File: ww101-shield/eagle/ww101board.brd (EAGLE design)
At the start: 64.5 x 73.1 mm, 62 parts

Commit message: before library update
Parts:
- added C15, C16, C17: 0.1uF, PatternAgents-ProtoPads:0603-CAP
- added R25: 0R, PatternAgents-ProtoPads:0603-RES
- moved C3 0.71 mm to (13.5, 17.8)
- moved C4 0.56 mm to (14.9, 17.8)
- moved R22 0.43 mm to (30.0, 11.7)
- moved C7 0.41 mm to (16.3, 17.8)
- moved C8 0.25 mm to (17.7, 17.8)
- moved C6 0.23 mm to (23.9, 1.52)
- moved C13 0.20 mm to (19.2, 1.78)
- moved C12 0.20 mm to (21.9, 17.8)
- moved C9 0.10 mm to (19.1, 17.8)
- moved C5 0.08 mm to (22.5, 1.52)
- moved D1 0.07 mm to (20.8, 3.10)
- moved C14 0.05 mm to (20.5, 17.8)
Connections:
- removed net VPWR: C1.2, C2.2, C3.2, C4.2, C5.1, C6.1, C8.2, C9.2, CLED0.A, CLED1.A, CLED2.A, CLED3.A, D1.ANNODE, JMP1.2, JP1.5, JPWR.2, LED1.A, LED2.A, PROX.A, R10.1, R18.2, R19.2, R2.3, R20.2, R21.2, R22.1, R30.1, R31.3, R9.1, U$7.19, U$7.43, U$7.47, U$7.8
- new net CAP-PSOC: R25.2, U$7.15
- new net VCC: C1.2, C15.1, C17.1, C2.2, C3.2, C4.2, C5.1, C6.1, C8.2, C9.2, CLED0.A, CLED1.A, CLED2.A, CLED3.A, D1.ANNODE, JMP1.2, JP1.5, JPWR.2, LED1.A, LED2.A, PROX.A, R10.1, R18.2, R19.2, R2.3, R20.2, R21.2, R22.1, R30.1, R31.3, R9.1, U$7.19, U$7.43, U$7.47, U$7.8
- net CAP-PROX: now also R25.1; no longer U$7.15
- net GND: now also C16.2, C17.2
- net POT: now also C16.1
- net XRES: now also C15.2
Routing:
- net VCC: track 0.00 -> 215.6 mm, vias 0 -> 2
- net VPWR: track 213.5 -> 0.00 mm, vias 2 -> 0
- net CAP-PROX: track 278.4 -> 268.3 mm
- net CAP-PSOC: track 0.00 -> 8.86 mm
- net POT: track 135.0 -> 138.5 mm
- net VDAC: track 105.2 -> 108.0 mm
- net XRES: track 74.5 -> 76.6 mm
- net GND: track 81.6 -> 81.1 mm, vias 94 -> 100

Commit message: the saturday night checkin of all of the V2.1 changes
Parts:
- removed JMP1: 0, PatternAgents-ProtoPads:JMP-3-NO-PTH-2.54
- removed JP1: 0, SparkFun-Connectors:1X05_LOCK
- removed JPWR: 0, PatternAgents-ProtoPads:JMP-3-NO-0603
- removed U$2: U8G-096-OLED, IOTExpert:096-SSD1306
- added J5: (no value), ww101board:JMP-3-NO-PTH-2.54
- added J6: U8G-096-OLED, ww101board:096-SSD1306
- added J7: 0, ww101board:1X05_LOCK
- added R32: (no value), ww101board:JMP-3-NO
- B0, B1, B2, B3: device PatternAgents-TouchWidgets:BUTTON_PASSIVE_10MM -> ww101board:BUTTON_PASSIVE_10MM
- C1, C10, C11, C12, C13, C14, C15, C16, C17, C2, C3, C4, C5, C6, C7, C8, C9: device PatternAgents-ProtoPads:0603-CAP -> ww101board:0603-CAP
- CLED0, CLED1, CLED2, CLED3, LED1, LED2, PROX: device adafruit:CHIP-LED0603 -> ww101board:CHIP-LED0603
- D1: device IOTExpert:ALS -> ww101board:ALS
- HUMIDITY: device IOTExpert:HUMIDITY -> ww101board:HUMIDITY
- MB1, MB2: device IOTExpert:SWITCH -> ww101board:SWITCH
- R1, R10, R12, R13, R14, R15, R16, R17, R18, R19, R20, R21, R22, R23, R24, R25, R3, R4, R5, R6, R7, R8, R9: device PatternAgents-ProtoPads:0603-RES -> ww101board:0603-RES
- R11: device varistor:R-5 -> ww101board:R-5
- R2: device pot:3386P -> ww101board:3386P
- R30: device PatternAgents-ProtoPads:JMP-3-1_2 -> ww101board:JMP-3-1_2
- R31: device PatternAgents-ProtoPads:JMP-3-2_3 -> ww101board:JMP-3-2_3
- U$1: device SparkFun-Boards:UNO_R3_SHIELD_NOLABELS -> ww101board:UNO_R3_SHIELD_NOLABELS
- U$7: device PatternAgents-Cypress:TQFP-7X7-48 -> ww101board:TQFP-7X7-48
- moved R18 0.13 mm to (14.8, 39.4)
- moved C5 0.08 mm to (22.5, 1.45)
- moved C6 0.08 mm to (23.9, 1.45)
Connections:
- net GND: now also J7.4; no longer JP1.4
- net MB1: now also J7.1; no longer JP1.1
- net MB2: now also J7.2; no longer JP1.2
- net N$14: now also J6.VDD; no longer U$2.VDD
- net N$17: now also J6.GND; no longer U$2.GND
- net SCL: now also J6.SCL; no longer U$2.SCL
- net SDA: now also J6.SDA; no longer U$2.SDA
- net V33: now also J5.3, R32.1; no longer JMP1.3, JPWR.3
- net V50: now also J5.1, R32.3; no longer JMP1.1, JPWR.1
- net VCC: now also J5.2, J7.5, R32.2; no longer JMP1.2, JP1.5, JPWR.2
- net XRES: now also J7.3; no longer JP1.3
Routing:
- net GND: track 81.1 -> 78.2 mm
- net V33: track 20.2 -> 18.4 mm
- net VCC: track 215.6 -> 217.1 mm
- net THERM-REF-HIGH: track 26.0 -> 27.2 mm
- added copper zone on layer 1, net V33
- added copper zone on layer 1, net V50
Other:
- board size 64.5 x 73.1 mm -> 64.8 x 73.3 mm
- board text added: "J1"
- board text added: "J2"
- board text added: "J3"
- board text added: "J4"
- board text added: "J6"
- board text added: "PSoC AFE Shield V2.1"
- board text removed: "PSoC AFE Shield V2.0"

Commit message: a bunch of minor tweaks
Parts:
- C17: value 0.1uF -> 10uF
- renumbered U$7 to U7
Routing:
- net V33: track 18.4 -> 22.3 mm
- net V50: track 20.7 -> 22.5 mm

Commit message: a bunch of updates
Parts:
- removed U$3: (no value), IOTExpert:CYPRESSLOGO
- added U$7: CYLOGO-SILK, ww101board:CYLOGO-SILK
- R18, R19, R20, R21: value 4.7K -> DNP
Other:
- board size 64.8 x 73.3 mm -> 65.8 x 74.3 mm
- board text added: "600-60500-01 REV2.1"
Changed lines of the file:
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@@
 <layer number="17" name="Pads" color="2" fill="1" visible="yes" active="yes"/>
 <layer number="18" name="Vias" color="2" fill="1" visible="yes" active="yes"/>
-<layer number="19" name="Unrouted" color="6" fill="1" visible="yes" active="yes"/>
-<layer number="20" name="Dimension" color="15" fill="1" visible="yes" active="yes"/>
+<layer number="19" name="Unrouted" color="6" fill="1" visible="no" active="yes"/>
+<layer number="20" name="Dimension" color="15" fill="1" visible="no" active="yes"/>
 <layer number="21" name="tPlace" color="7" fill="1" visible="yes" active="yes"/>
 <layer number="22" name="bPlace" color="7" fill="1" visible="yes" active="yes"/>
@@
 <board>
 <plain>
-<wire x1="-5.7404" y1="-9.1694" x2="59.055" y2="-9.1694" width="0" layer="20"/>
-<wire x1="59.055" y1="-9.1694" x2="59.055" y2="64.135" width="0" layer="20"/>
-<wire x1="59.055" y1="64.135" x2="-5.7404" y2="64.135" width="0" layer="20"/>
-<wire x1="-5.7404" y1="64.135" x2="-5.7404" y2="-9.1694" width="0" layer="20"/>
+<wire x1="-6.2484" y1="-9.6774" x2="59.563" y2="-9.6774" width="0" layer="20"/>
+<wire x1="59.563" y1="-9.6774" x2="59.563" y2="64.643" width="0" layer="20"/>
+<wire x1="59.563" y1="64.643" x2="-6.2484" y2="64.643" width="0" layer="20"/>
+<wire x1="-6.2484" y1="64.643" x2="-6.2484" y2="-9.6774" width="0" layer="20"/>
 <text x="36.164521875" y="24.462740625" size="1.016" layer="25" font="vector" ratio="15" rot="R90">V33</text>
 <text x="55.095140625" y="27.040840625" size="1.016" layer="25" font="vector" ratio="15" rot="R180">V33</text>
@@
 <wire x1="20.7797375" y1="-1.33858125" x2="20.99818125" y2="-1.33858125" width="0.1524" layer="21"/>
 <wire x1="20.99818125" y1="-1.33858125" x2="21.638259375" y2="-1.978659375" width="0.1524" layer="21"/>
+<text x="17.266921875" y="-7.929884375" size="1.27" layer="26" ratio="10" rot="MR0">600-60500-01 REV2.1</text>
 </plain>
 <attributes>
@@
 <attribute name="VALUE" x="21.5138" y="16.2306" size="0.6096" layer="27" font="vector" ratio="15" rot="R90" align="top-left"/>
 </element>
-<element name="R18" library="ww101board" package="0603-RES" value="4.7K" x="14.7574" y="39.4208" smashed="yes">
+<element name="R18" library="ww101board" package="0603-RES" value="DNP" x="14.7574" y="39.4208" smashed="yes">
 <attribute name="NAME" x="16.494759375" y="40.8914625" size="0.8128" layer="25" font="vector" ratio="15" rot="R270"/>
 <attribute name="VALUE" x="13.2334" y="37.7698" size="0.6096" layer="27" font="vector" ratio="15"/>
 </element>
-<element name="R19" library="ww101board" package="0603-RES" value="4.7K" x="14.732" y="35.6362" locked="yes" smashed="yes" rot="MR180">
+<element name="R19" library="ww101board" package="0603-RES" value="DNP" x="14.732" y="35.6362" locked="yes" smashed="yes" rot="MR180">
 <attribute name="NAME" x="10.7188" y="35.8902" size="0.8128" layer="26" font="vector" ratio="15" rot="MR180"/>
 <attribute name="VALUE" x="13.208" y="37.2872" size="0.6096" layer="28" font="vector" ratio="15" rot="MR180"/>
 </element>
-<element name="R20" library="ww101board" package="0603-RES" value="4.7K" x="14.7574" y="38.0238" locked="yes" smashed="yes">
+<element name="R20" library="ww101board" package="0603-RES" value="DNP" x="14.7574" y="38.0238" locked="yes" smashed="yes">
 <attribute name="NAME" x="17.205959375" y="35.829240625" size="0.8128" layer="25" font="vector" ratio="15" rot="R90"/>
 <attribute name="VALUE" x="13.2334" y="36.3728" size="0.6096" layer="27" font="vector" ratio="15"/>
 </element>
-<element name="R21" library="ww101board" package="0603-RES" value="4.7K" x="14.732" y="36.8554" locked="yes" smashed="yes" rot="MR180">
+<element name="R21" library="ww101board" package="0603-RES" value="DNP" x="14.732" y="36.8554" locked="yes" smashed="yes" rot="MR180">
 <attribute name="NAME" x="10.6426" y="37.1856" size="0.8128" layer="26" font="vector" ratio="15" rot="MR180"/>
 <attribute name="VALUE" x="13.208" y="38.5064" size="0.6096" layer="28" font="vector" ratio="15" rot="MR180"/>
 </element>
 <element name="U$1" library="ww101board" package="UNO_R3_SHIELD_NOLABELS" value="ARDUINO_R3_SHIELDNOLABELS" x="-0.03" y="0.01" locked="yes"/>
-<element name="U$3" library="IOTExpert" package="CYPRESSLOGO" value="" x="52.0573" y="7.2009" rot="R90"/>
 <element name="R22" library="ww101board" package="0603-RES" value="10K" x="29.96691875" y="11.69161875" smashed="yes" rot="R180">
 <attribute name="NAME" x="31.1023" y="13.243559375" size="0.8128" layer="25" font="vector" ratio="15" rot="R180"/>
@@
 <attribute name="VALUE" x="37.337996875" y="28.26511875" size="0.6096" layer="27" font="vector" ratio="15" rot="R90"/>
 </element>
+<element name="U$7" library="ww101board" package="CYLOGO-SILK" value="CYLOGO-SILK" x="58.399678125" y="-8.453115625" rot="R90"/>
 </elements>
 <signals>

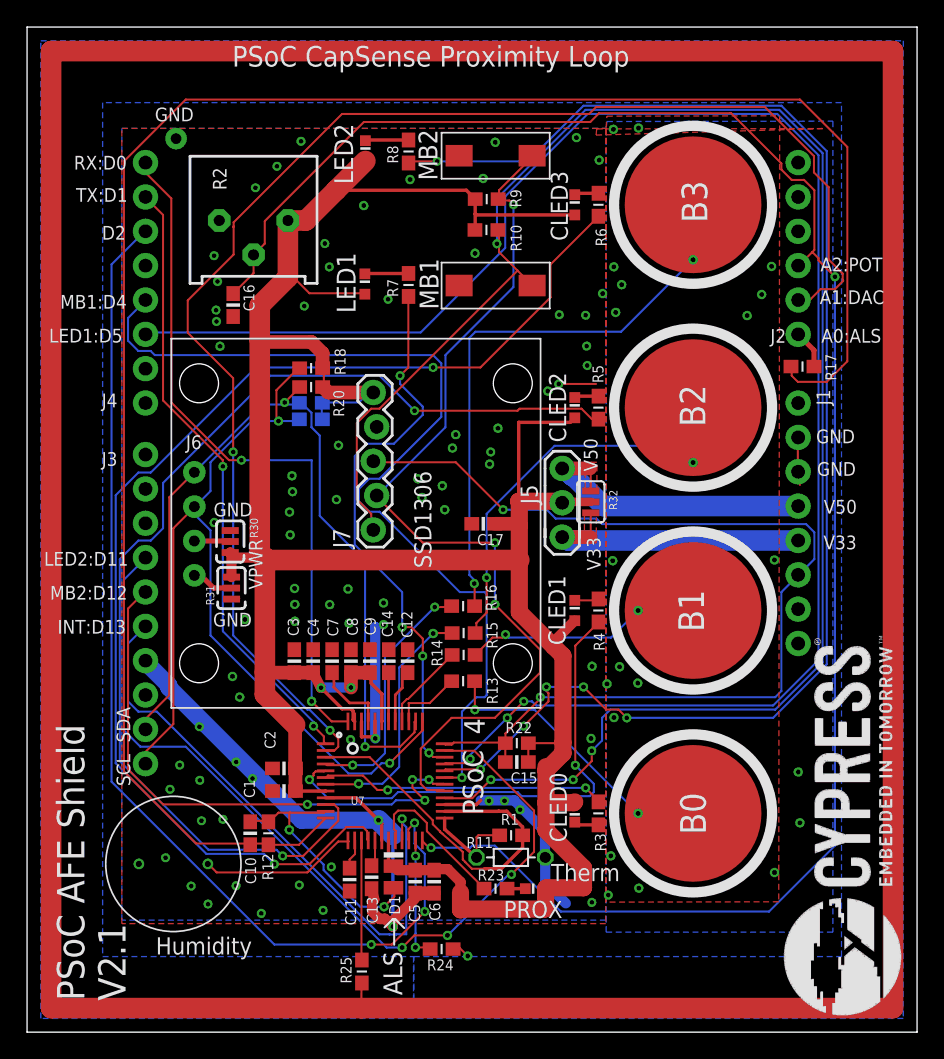
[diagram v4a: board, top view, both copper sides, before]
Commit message: updates to 2.1 board based on GJL inputs
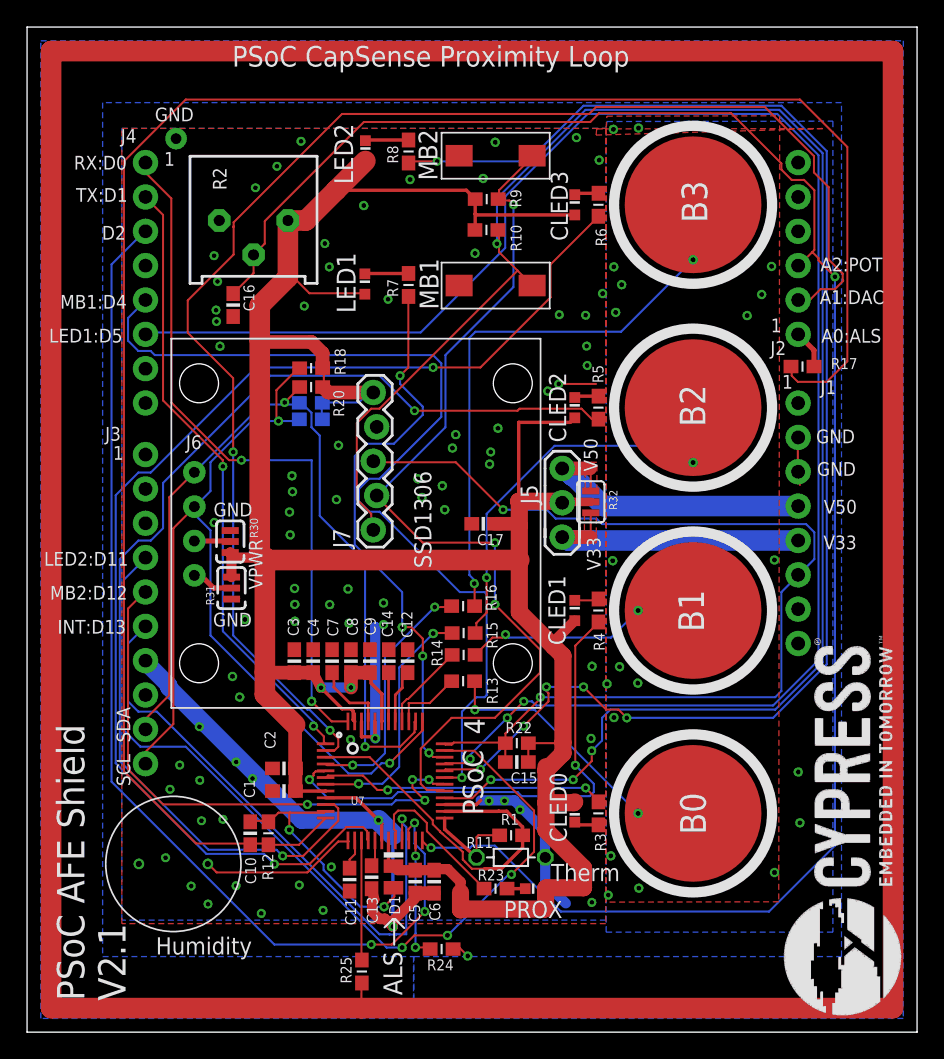
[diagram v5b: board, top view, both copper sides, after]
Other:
- board text added: "1"
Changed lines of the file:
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@@
 <grid distance="0.1" unitdist="mil" unit="mil" style="lines" multiple="1" display="no" altdistance="0.025" altunitdist="inch" altunit="inch"/>
 <layers>
-<layer number="1" name="Top" color="4" fill="1" visible="yes" active="yes"/>
+<layer number="1" name="Top" color="4" fill="1" visible="no" active="yes"/>
 <layer number="2" name="Route2" color="1" fill="3" visible="no" active="no"/>
 <layer number="3" name="Route3" color="4" fill="3" visible="no" active="no"/>
@@
 <layer number="19" name="Unrouted" color="6" fill="1" visible="no" active="yes"/>
 <layer number="20" name="Dimension" color="15" fill="1" visible="no" active="yes"/>
-<layer number="21" name="tPlace" color="7" fill="1" visible="yes" active="yes"/>
-<layer number="22" name="bPlace" color="7" fill="1" visible="yes" active="yes"/>
+<layer number="21" name="tPlace" color="7" fill="1" visible="no" active="yes"/>
+<layer number="22" name="bPlace" color="7" fill="1" visible="no" active="yes"/>
 <layer number="23" name="tOrigins" color="15" fill="1" visible="no" active="yes"/>
 <layer number="24" name="bOrigins" color="15" fill="1" visible="no" active="yes"/>
-<layer number="25" name="tNames" color="7" fill="1" visible="yes" active="yes"/>
-<layer number="26" name="bNames" color="7" fill="1" visible="yes" active="yes"/>
-<layer number="27" name="tValues" color="7" fill="1" visible="yes" active="yes"/>
-<layer number="28" name="bValues" color="7" fill="1" visible="yes" active="yes"/>
-<layer number="29" name="tStop" color="7" fill="3" visible="yes" active="yes"/>
-<layer number="30" name="bStop" color="7" fill="6" visible="yes" active="yes"/>
-<layer number="31" name="tCream" color="7" fill="4" visible="yes" active="yes"/>
-<layer number="32" name="bCream" color="7" fill="5" visible="yes" active="yes"/>
+<layer number="25" name="tNames" color="7" fill="1" visible="no" active="yes"/>
+<layer number="26" name="bNames" color="7" fill="1" visible="no" active="yes"/>
+<layer number="27" name="tValues" color="7" fill="1" visible="no" active="yes"/>
+<layer number="28" name="bValues" color="7" fill="1" visible="no" active="yes"/>
+<layer number="29" name="tStop" color="7" fill="3" visible="no" active="yes"/>
+<layer number="30" name="bStop" color="7" fill="6" visible="no" active="yes"/>
+<layer number="31" name="tCream" color="7" fill="4" visible="no" active="yes"/>
+<layer number="32" name="bCream" color="7" fill="5" visible="no" active="yes"/>
 <layer number="33" name="tFinish" color="6" fill="3" visible="no" active="yes"/>
 <layer number="34" name="bFinish" color="6" fill="6" visible="no" active="yes"/>
@@
 <text x="54.97068125" y="34.881821875" size="1.016" layer="25" font="vector" ratio="15" rot="R180">GND</text>
 <text x="6.078221875" y="58.686703125" size="1.016" layer="25" font="vector" ratio="15" rot="R180">GND</text>
-<text x="52.125878125" y="37.8434625" size="1.016" layer="25" font="vector" ratio="15" rot="R270">J1</text>
-<text x="49.880525" y="42.31131875" size="1.016" layer="25" font="vector" ratio="15" rot="R180">J2</text>
-<text x="-0.731521875" y="32.194496875" size="1.016" layer="25" font="vector" ratio="15">J3</text>
-<text x="-0.731521875" y="36.52265625" size="1.016" layer="25" font="vector" ratio="15">J4</text>
+<text x="53.5787625" y="38.519103125" size="1.016" layer="25" font="vector" ratio="15" rot="R180">J1</text>
+<text x="49.880525" y="41.412159375" size="1.016" layer="25" font="vector" ratio="15" rot="R180">J2</text>
+<text x="-0.474984375" y="34.05631875" size="1.016" layer="25" font="vector" ratio="15">J3</text>
+<text x="0.678178125" y="56.08319375" size="1.016" layer="25" font="vector" ratio="15">J4</text>
 <text x="5.4991" y="33.434015625" size="1.016" layer="25" font="vector" ratio="15">J6</text>
 <wire x1="20.89911875" y1="-1.33858125" x2="20.89911875" y2="-3.21818125" width="0.1524" layer="21"/>
@@
 <wire x1="20.99818125" y1="-1.33858125" x2="21.638259375" y2="-1.978659375" width="0.1524" layer="21"/>
 <text x="17.266921875" y="-7.929884375" size="1.27" layer="26" ratio="10" rot="MR0">600-60500-01 REV2.1</text>
+<text x="0.101596875" y="32.644078125" size="1.016" layer="25" font="vector" ratio="15">1</text>
+<text x="3.881115625" y="54.3839375" size="1.016" layer="25" font="vector" ratio="15">1</text>
+<text x="48.742596875" y="42.07255625" size="1.016" layer="25" font="vector" ratio="15">1</text>
+<text x="49.575715625" y="37.901878125" size="1.016" layer="25" font="vector" ratio="15">1</text>
 </plain>
 <attributes>
@@
 </element>
 <element name="R17" library="ww101board" package="0603-RES" value="0" x="51.09" y="39.54" locked="yes" smashed="yes" rot="R180">
-<attribute name="NAME" x="52.781378125" y="40.475340625" size="0.8128" layer="25" font="vector" ratio="15" rot="R270"/>
+<attribute name="NAME" x="53.184621875" y="39.352396875" size="0.8128" layer="25" font="vector" ratio="15"/>
 <attribute name="VALUE" x="52.614" y="41.191" size="0.6096" layer="27" font="vector" ratio="15" rot="R180"/>
 </element>

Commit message: a number of small changes to the 2.2 baord
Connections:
- net UARTRX: now also U7.48; no longer U7.1
- net UARTTX: now also U7.1; no longer U7.48
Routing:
- net UARTRX: track 46.0 -> 50.4 mm, vias 2 -> 3
- net UARTTX: track 51.9 -> 48.5 mm
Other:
- board text added: "600-60500-01 REV2.2"
- board text added: "BAR CODE"
- board text added: "PSoC AFE Shield V2.2"
- board text added: "QR CODE"
- board text removed: "600-60500-01 REV2.1"
- board text removed: "PSoC AFE Shield V2.1"
